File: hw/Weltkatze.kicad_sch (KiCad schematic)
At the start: 0 parts

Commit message: Rest of the owl
Finish major layout, minor tweaks can be made
E.g. rotating the LEDs so they look pretty

Still need to make it so the inner PCB is manufacturable
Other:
- sheet Logic ports: added none; removed ESP_DN, ESP_DP
- sheet Power ports: added USBD_N, USBD_P, VBAT_MON; removed VBAT
- sheet USB ports: added USBD_N, USBD_P; removed USB_DN, USB_DP
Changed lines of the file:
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@@
 		(comment 1 "A light up Zigbee kitty")
 	)
-	(junction
-		(at 134.62 84.455)
-		(diameter 0)
-		(color 0 0 0 0)
-	)
-	(wire
-		(pts
-			(xy 116.205 90.17) (xy 123.19 90.17)
-		)
-		(stroke
-			(width 0)
-			(type default)
-		)
-	)
-	(wire
-		(pts
-			(xy 134.62 74.93) (xy 134.62 84.455)
-		)
-		(stroke
-			(width 0)
-			(type default)
-		)
-	)
-	(wire
-		(pts
-			(xy 116.205 81.28) (xy 124.46 81.28)
-		)
-		(stroke
-			(width 0)
-			(type default)
-		)
-	)
-	(wire
-		(pts
-			(xy 116.205 87.63) (xy 123.19 87.63)
-		)
-		(stroke
-			(width 0)
-			(type default)
-		)
-	)
-	(wire
-		(pts
-			(xy 134.62 84.455) (xy 134.62 85.09)
-		)
-		(stroke
-			(width 0)
-			(type default)
-		)
-	)
-	(wire
-		(pts
-			(xy 124.46 67.31) (xy 125.095 67.31)
-		)
-		(stroke
-			(width 0)
-			(type default)
-		)
-	)
-	(wire
-		(pts
-			(xy 147.32 86.36) (xy 152.4 86.36)
-		)
-		(stroke
-			(width 0)
-			(type default)
-		)
-	)
-	(wire
-		(pts
-			(xy 124.46 81.28) (xy 124.46 67.31)
+	(wire
+		(pts
+			(xy 104.14 78.74) (xy 104.14 71.12)
+		)
+		(stroke
+			(width 0)
+			(type default)
+		)
+	)
+	(wire
+		(pts
+			(xy 106.68 78.74) (xy 106.68 73.66)
+		)
+		(stroke
+			(width 0)
+			(type default)
+		)
+	)
+	(wire
+		(pts
+			(xy 106.68 73.66) (xy 125.73 73.66)
+		)
+		(stroke
+			(width 0)
+			(type default)
+		)
+	)
+	(wire
+		(pts
+			(xy 104.14 71.12) (xy 125.73 71.12)
+		)
+		(stroke
+			(width 0)
+			(type default)
+		)
+	)
+	(wire
+		(pts
+			(xy 101.6 67.31) (xy 125.73 67.31)
+		)
+		(stroke
+			(width 0)
+			(type default)
+		)
+	)
+	(wire
+		(pts
+			(xy 135.89 74.93) (xy 135.89 85.09)
+		)
+		(stroke
+			(width 0)
+			(type default)
+		)
+	)
+	(wire
+		(pts
+			(xy 147.32 87.63) (xy 152.4 87.63)
+		)
+		(stroke
+			(width 0)
+			(type default)
+		)
+	)
+	(wire
+		(pts
+			(xy 101.6 67.31) (xy 101.6 78.74)
 		)
 		(stroke
@@
 	)
 	(sheet
-		(at 123.19 84.455)
+		(at 123.19 85.09)
 		(size 24.13 12.7)
 		(fields_autoplaced yes)
@@
 		)
 		(property "Sheetname" "Logic"
-			(at 123.19 83.7434 0)
+			(at 123.19 84.3784 0)
 			(effects
 				(font
@@
 		)
 		(property "Sheetfile" "logic.kicad_sch"
-			(at 123.19 97.7396 0)
+			(at 123.19 98.3746 0)
 			(effects
 				(font
@@
 		)
 		(property "Field2" ""
-			(at 123.19 84.455 0)
+			(at 123.19 85.09 0)
 			(effects
 				(font
@@
 			)
 		)
-		(pin "ESP_DP" input
-			(at 123.19 87.63 180)
-			(effects
-				(font
-					(size 1.27 1.27)
-				)
-				(justify left)
-			)
-		)
 		(pin "ESP_PWM" input
-			(at 147.32 86.36 0)
-			(effects
-				(font
-					(size 1.27 1.27)
-				)
-				(justify right)
-			)
-		)
-		(pin "ESP_DN" input
-			(at 123.19 90.17 180)
-			(effects
-				(font
-					(size 1.27 1.27)
-				)
-				(justify left)
+			(at 147.32 87.63 0)
+			(effects
+				(font
+					(size 1.27 1.27)
+				)
+				(justify right)
 			)
 		)
 		(pin "VBAT_MON" input
-			(at 134.62 84.455 90)
+			(at 135.89 85.09 90)
 			(effects
 				(font
@@
 			)
 		)
-		(pin "USB_DP" input
-			(at 116.205 87.63 0)
-			(effects
-				(font
-					(size 1.27 1.27)
-				)
-				(justify right)
-			)
-		)
 		(pin "USB_VBUS" input
-			(at 116.205 81.28 0)
-			(effects
-				(font
-					(size 1.27 1.27)
-				)
-				(justify right)
-			)
-		)
-		(pin "USB_DN" input
-			(at 116.205 90.17 0)
+			(at 101.6 78.74 90)
+			(effects
+				(font
+					(size 1.27 1.27)
+				)
+				(justify right)
+			)
+		)
+		(pin "USBD_N" input
+			(at 106.68 78.74 90)
+			(effects
+				(font
+					(size 1.27 1.27)
+				)
+				(justify right)
+			)
+		)
+		(pin "USBD_P" input
+			(at 104.14 78.74 90)
 			(effects
 				(font
@@
 	)
 	(sheet
-		(at 152.4 78.74)
+		(at 152.4 80.01)
 		(size 17.78 10.795)
 		(fields_autoplaced yes)
@@
 		)
 		(property "Sheetname" "LEDs"
-			(at 152.4 78.0284 0)
+			(at 152.4 79.2984 0)
 			(effects
 				(font
@@
 		)
 		(property "Sheetfile" "led.kicad_sch"
-			(at 152.4 90.1196 0)
+			(at 152.4 91.3896 0)
 			(effects
 				(font
@@
 		)
 		(pin "LED_DIN" input
-			(at 152.4 86.36 180)
+			(at 152.4 87.63 180)
 			(effects
 				(font
@@
 	)
 	(sheet
-		(at 125.095 63.5)
+		(at 125.73 63.5)
 		(size 15.875 11.43)
 		(fields_autoplaced yes)
@@
 		)
 		(property "Sheetname" "Power"
-			(at 125.095 62.7884 0)
+			(at 125.73 62.7884 0)
 			(effects
 				(font
@@
 		)
 		(property "Sheetfile" "Power.kicad_sch"
-			(at 125.095 75.5146 0)
+			(at 125.73 75.5146 0)
 			(effects
 				(font
@@
 		)
 		(pin "USB_VBUS" input
-			(at 125.095 67.31 180)
+			(at 125.73 67.31 180)
 			(effects
 				(font
@@
 			)
 		)
-		(pin "VBAT" input
-			(at 134.62 74.93 270)
-			(effects
-				(font
+		(pin "VBAT_MON" input
+			(at 135.89 74.93 270)
+			(effects
+				(font
+					(size 1.27 1.27)
+				)
+				(justify left)
+			)
+		)
+		(pin "USBD_N" input
+			(at 125.73 73.66 180)
+			(effects
+				(font
+					(size 1.27 1.27)
+				)
+				(justify left)
+			)
+		)
+		(pin "USBD_P" input
+			(at 125.73 71.12 180)
+			(effects
+				(font

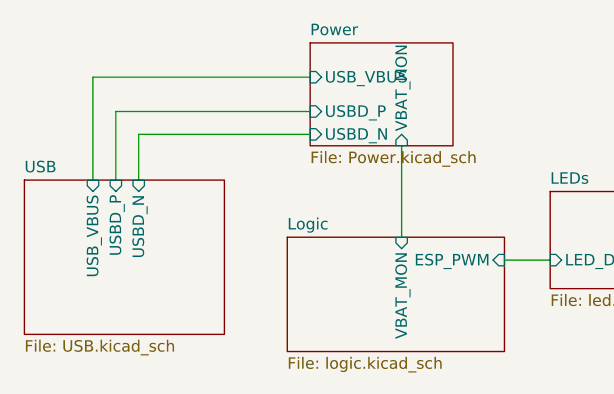
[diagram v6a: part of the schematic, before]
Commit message: V1 REV1 Final!
I consider this design finished, as such I've submitted it to JLCPCB

I converted to a 6L pcb because its cheaper, in.3 and in.4 have no copper
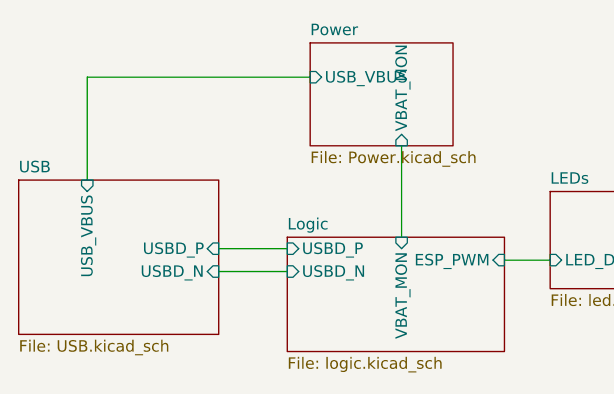
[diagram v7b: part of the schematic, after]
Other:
- sheet Logic ports: added USBD_N, USBD_P; removed none
- sheet Power ports: added none; removed USBD_N, USBD_P
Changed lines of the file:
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@@
 	(wire
 		(pts
-			(xy 104.14 78.74) (xy 104.14 71.12)
-		)
-		(stroke
-			(width 0)
-			(type default)
-		)
-	)
-	(wire
-		(pts
-			(xy 106.68 78.74) (xy 106.68 73.66)
-		)
-		(stroke
-			(width 0)
-			(type default)
-		)
-	)
-	(wire
-		(pts
-			(xy 106.68 73.66) (xy 125.73 73.66)
-		)
-		(stroke
-			(width 0)
-			(type default)
-		)
-	)
-	(wire
-		(pts
-			(xy 104.14 71.12) (xy 125.73 71.12)
-		)
-		(stroke
-			(width 0)
-			(type default)
-		)
-	)
-	(wire
-		(pts
-			(xy 101.6 67.31) (xy 125.73 67.31)
+			(xy 115.57 88.9) (xy 123.19 88.9)
+		)
+		(stroke
+			(width 0)
+			(type default)
+		)
+	)
+	(wire
+		(pts
+			(xy 115.57 86.36) (xy 123.19 86.36)
+		)
+		(stroke
+			(width 0)
+			(type default)
+		)
+	)
+	(wire
+		(pts
+			(xy 100.965 67.31) (xy 125.73 67.31)
 		)
 		(stroke
@@
 	(wire
 		(pts
-			(xy 101.6 67.31) (xy 101.6 78.74)
+			(xy 100.965 67.31) (xy 100.965 78.74)
 		)
 		(stroke
@@
 				)
 				(justify right)
+			)
+		)
+		(pin "USBD_P" input
+			(at 123.19 86.36 180)
+			(effects
+				(font
+					(size 1.27 1.27)
+				)
+				(justify left)
+			)
+		)
+		(pin "USBD_N" input
+			(at 123.19 88.9 180)
+			(effects
+				(font
+					(size 1.27 1.27)
+				)
+				(justify left)
 			)
 		)
@@
 	)
 	(sheet
-		(at 93.98 78.74)
+		(at 93.345 78.74)
 		(size 22.225 17.145)
 		(fields_autoplaced yes)
@@
 		)
 		(property "Sheetname" "USB"
-			(at 93.98 78.0284 0)
+			(at 93.345 78.0284 0)
 			(effects
 				(font
@@
 		)
 		(property "Sheetfile" "USB.kicad_sch"
-			(at 93.98 96.4696 0)
+			(at 93.345 96.4696 0)
 			(effects
 				(font
@@
 		)
 		(pin "USB_VBUS" input
-			(at 101.6 78.74 90)
+			(at 100.965 78.74 90)
 			(effects
 				(font
@@
 		)
 		(pin "USBD_N" input
-			(at 106.68 78.74 90)
+			(at 115.57 88.9 0)
 			(effects
 				(font
@@
 		)
 		(pin "USBD_P" input
-			(at 104.14 78.74 90)
+			(at 115.57 86.36 0)
 			(effects
 				(font
@@
 			(effects
 				(font
-					(size 1.27 1.27)
-				)
-				(justify left)
-			)
-		)
-		(pin "USBD_N" input
-			(at 125.73 73.66 180)
-			(effects
-				(font
-					(size 1.27 1.27)
-				)
-				(justify left)
-			)
-		)
-		(pin "USBD_P" input
-			(at 125.73 71.12 180)
-			(effects
-				(font
